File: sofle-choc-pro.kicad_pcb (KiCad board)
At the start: 4 copper layers, 129 x 119 mm, 198 parts, among them J1 Connector, USB-TYPE-C-16P, J2 Connector, USB-TYPE-C-16P, J3 OLED 128x32 / nice!view, SW1 BOOT, SW10 F0, SW11 F1, SW12 F2, SW13 F3, SW14 F4, SW15 F5, SW16 F6 Choc/EC11, SW2 RESET, SW20 N0, SW21 N1, SW22 N2, SW23 N3, SW24 N4, SW25 N5, SW30 T0, SW31 T1, SW32 T2, SW33 T3, SW34 T4, SW35 T5, SW40 H0, SW41 H1, SW42 H2, SW43 H3, SW44 H4, SW45 H5, SW50 B0, SW51 B1, SW52 B2, SW53 B3, SW54 B4, SW55 B5, SW60 TH0, SW61 TH1, SW62 TH2, SW63 TH3, SW64 TH4, SW65 TH5 Choc/EC11, U1 RP2040, U2 SRV05-4, U3 W25Q128, U4 SRV05-4, U5 AP2112K-3.3, U6 SN74LV1T34DBVR, X1 ABM8-272-T3

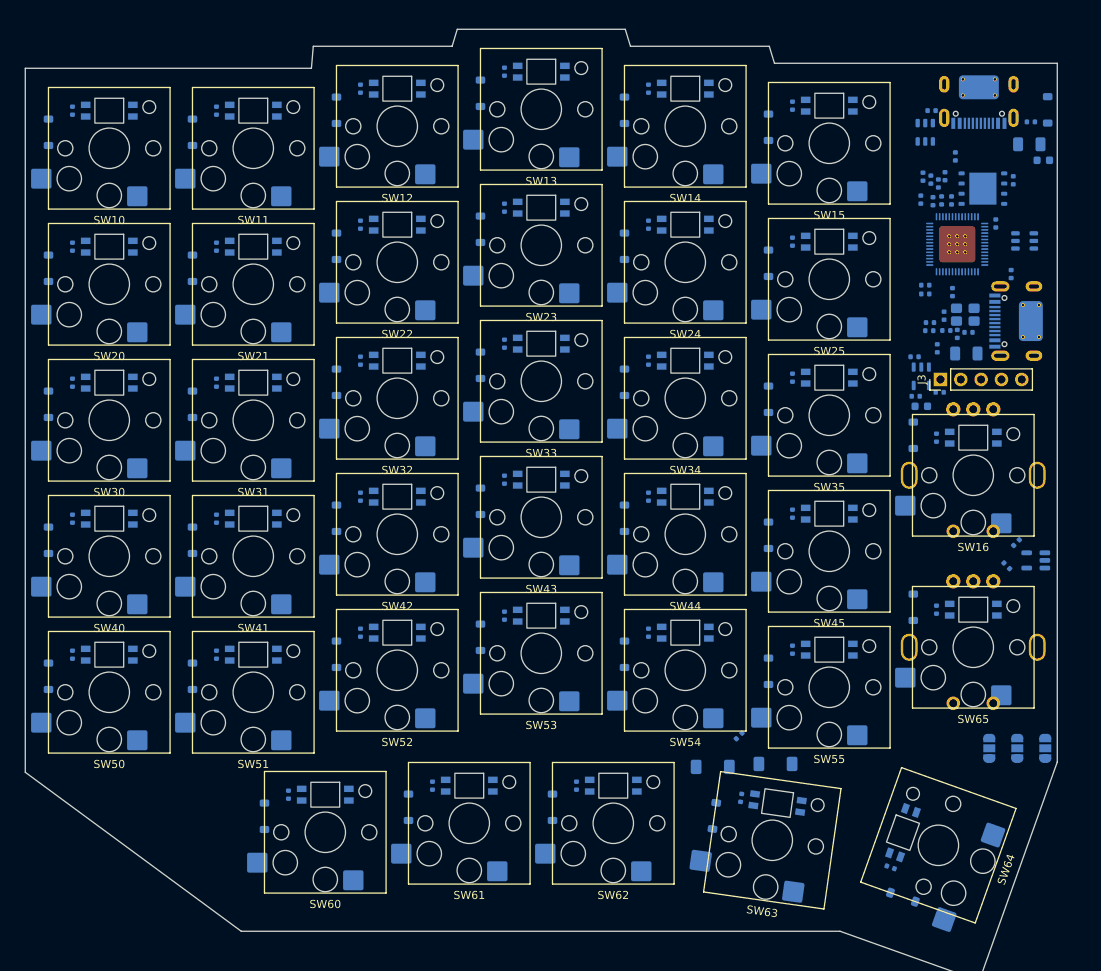
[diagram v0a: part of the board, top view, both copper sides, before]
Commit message: feat(pcb): swap usb-c and esd parts, fix nets, rules and silkscreen
Moves both USB-C ports to the part every reference board uses, shrinks the
ESD arrays and cleans up the nets, rules and silkscreen around them. The
board passes ERC and DRC with no errors and no schematic parity issues.

- USB-C J1/J2 are now HRO TYPE-C-31-M-12 (LCSC C165948), the connector the
  RP2040 design guide, Corne v4, Djinn, Ferris and sea-picro all use, with
  its real 3D model and a project footprint whose pad numbers match our
  symbol; both sit 0.49 mm proud of the board edge, per its datasheet
- ESD arrays are USBLC6-2P6 in SOT-563 (2.0 x 2.5 mm against 3.1 x 2.1),
  and their two channels now carry each data line through the part, which
  is the layout ST and TI ask for
- USB nets are named per segment so each side of R7/R8 is its own net:
  D+/D- from the connector, USB_P/USB_N into the MCU
- R7/R8 moved 12.7 mm clear of U1 so the MCU-side labels have a wire to sit
  on instead of printing over the chip symbol
- protection parts sit at the connectors: fuse 2.5 mm from the 5 V pad,
  ESD 1.5 to 2.0 mm from the data pads, diode right after the fuse
- fuses raised to 1.1 A (LCSC C126818): 37 LEDs at the planned brightness
  draw about 0.8 A through one half's fuse, which would trip a 500 mA part

Under the hood:

- design rules follow JLCPCB's published limits: 0.3 mm copper to edge,
  0.4 mm minimum via, 0.15 mm silkscreen lines and 1.0 mm text
- one diff pair rule per pair, with spacing checked outside the fan-out and
  length across the whole net; a shared rule compared nets across ports,
  and a rule condition split over two lines was silently ignored
- no pair rule on the link port: it is one-wire serial, and LINK_D_N never
  reaches the MCU
- GND plane moved to the inner layer next to the parts, so USB, ESD and
  decoupling reference solid ground
- crystal keep-out now covers the power plane only: Abracon and Raspberry
  Pi ask for short traces, not cleared ground, and the plane a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
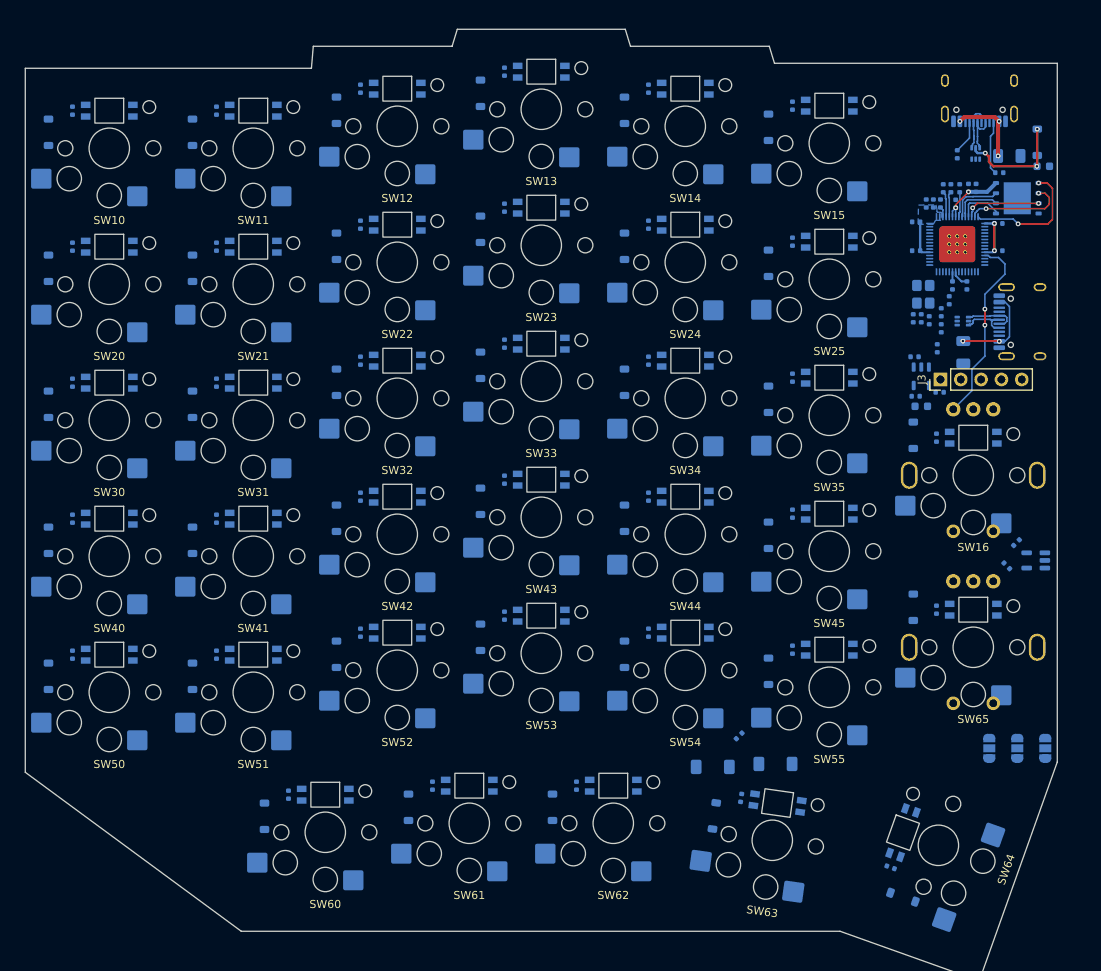
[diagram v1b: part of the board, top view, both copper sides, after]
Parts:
- F1, F2: value 500mA -> 1.1A
- J1, J2: footprint PCM_JLCPCB:TYPE-C-SMD_HX-TYPE-C-16PIN -> my-soffle:USB_C_Receptacle_HRO_TYPE-C-31-M-12_MergedPads
- U2, U4: value SRV05-4 -> USBLC6-2P6; footprint PCM_JLCPCB:SOT-23-6_L2.9-W1.6-P0.95-LS2.9-BL -> Package_TO_SOT_SMD:SOT-563
- U3: value W25Q128 -> W25Q128JVPIQ
- moved U2 12.7 mm to (166.7, 93.6), turned to 0 degrees
- moved C13 8.85 mm to (160.9, 84.8), turned to 180 degrees
- moved R6 7.48 mm to (171.2, 75.0)
- moved U4 6.83 mm to (168.3, 72.7), turned to 90 degrees
- moved R5 6.33 mm to (166.0, 72.8), turned to -90 degrees
- moved X1 5.84 mm to (161.8, 90.2), turned to 90 degrees
- moved R11 5.84 mm to (160.5, 93.2), turned to -90 degrees
- moved C14 5.59 mm to (160.9, 81.2), turned to 180 degrees
- moved C12 5.31 mm to (167.2, 89.1), turned to -90 degrees
- moved C6 5.06 mm to (166.3, 77.0)
- moved C3 4.75 mm to (168.3, 77.0)
- moved U3 4.47 mm to (173.5, 78.2)
- moved C15 4.26 mm to (167.4, 77.0)
- moved D1 4.25 mm to (176.0, 71.2), turned to -90 degrees
- moved C1 4.23 mm to (164.0, 92.5), turned to 90 degrees
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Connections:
- net USB_MCU_N renamed USB_N
- net USB_MCU_P renamed USB_P
- J1 pad A6: D_USB_P -> D+
- J1 pad A7: D_USB_N -> D-
- J1 pad B6: D_USB_P -> D+
- J1 pad B7: D_USB_N -> D-
- R7 pad 1: D_USB_P -> D+
- R8 pad 1: D_USB_N -> D-
- U2 pad 3: unconnected-(U2-I/O-Pad3) -> LINK_D_N
- U2 pad 6: unconnected-(U2-I/O-Pad6) -> LINK_D_P
- U4 pad 1: D_USB_P -> D+
- U4 pad 3: unconnected-(U4-I/O-Pad3) -> D-
- U4 pad 4: unconnected-(U4-I/O-Pad4) -> D-
- U4 pad 6: D_USB_N -> D+
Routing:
- net GP8: track 0.00 -> 23.8 mm, vias 0 -> 2
- net +3.3V: track 0.00 -> 21.9 mm, vias 0 -> 4
- net SS: track 0.00 -> 15.8 mm, vias 0 -> 2
- net +5V: track 0.00 -> 13.9 mm, vias 0 -> 3
- net SD1: track 0.00 -> 12.8 mm, vias 0 -> 2
- net LINK_VBUS: track 0.00 -> 11.4 mm, vias 0 -> 2
- net VBUS: track 0.00 -> 9.73 mm, vias 0 -> 3
- net SD2: track 0.00 -> 9.63 mm, vias 0 -> 2
- net LINK_D_P: track 0.00 -> 6.92 mm
- net Net-(J1-CC2): track 0.00 -> 6.82 mm
- net SD3: track 0.00 -> 6.63 mm
- net LINK_D_N: track 0.00 -> 6.50 mm
- net D-: track 0.00 -> 6.04 mm
- net D+: track 0.00 -> 6.03 mm
- net CLK: track 0.00 -> 5.98 mm
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- added copper zone on B.Cu, net +3.3V
- added copper zone on In1.Cu, net +3.3V
- added copper zone on In1.Cu, net +5V
- added copper zone on In2.Cu, net GND
- removed copper zone on In2.Cu, net +3.3V
- removed copper zone on In2.Cu, net +5V
- removed copper zone on In1.Cu, net GND

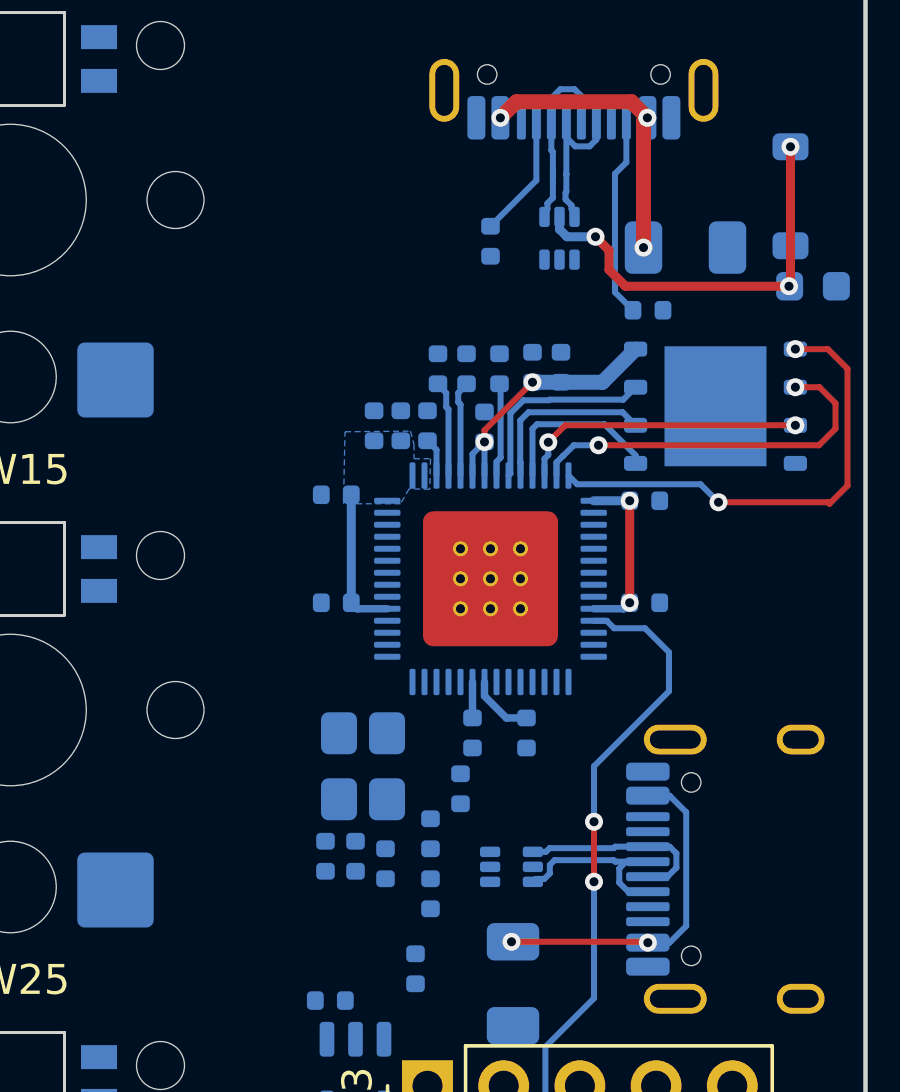
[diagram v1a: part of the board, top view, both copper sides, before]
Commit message: fix(pcb): drop the dead link d- pad and exempt the esd fan-out
The link between halves is one-wire serial, so D- stops at the ESD array.
Both of its pads carried the net, which left KiCad asking for copper between
two pins the chip already joins inside. Now only the pad the connector
reaches is wired, and the other is a no-connect.

- U2 pin 3 disconnected in the schematic and on the board: four fewer
  unconnected items, and no more phantom pad-to-pad link
- D+/D- spacing rule now skips U4's courtyard as well as J1's and U1's,
  since the ESD array's two data pins sit 2.3 mm apart and set the gap

Also carries the USB and link routing done in KiCad since the last commit.

ERC 0 errors. DRC 0 errors, 0 parity issues. One skew flag remains on the
host pair (0.23 mm), to even out once that pair is finished.
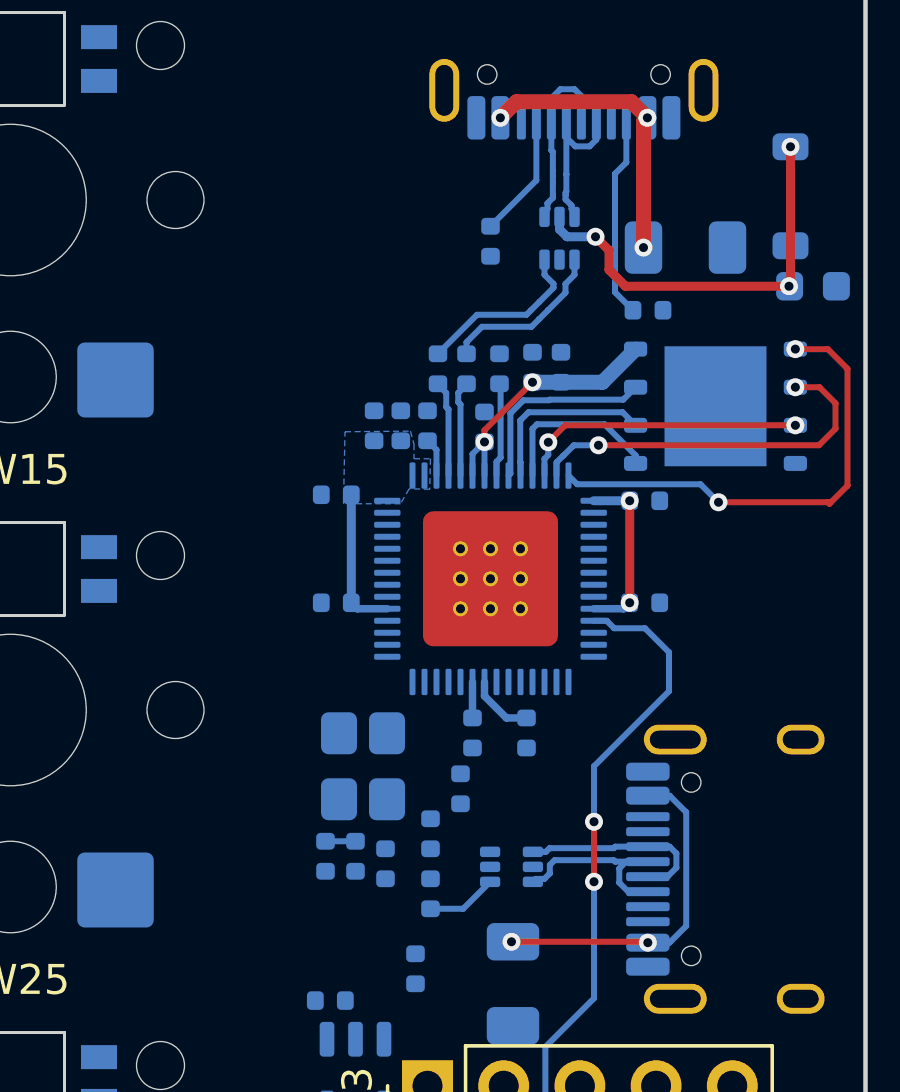
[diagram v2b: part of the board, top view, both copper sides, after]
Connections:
- U2 pad 3: LINK_D_N -> (no net)
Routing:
- net D-: track 6.04 -> 11.9 mm
- net D+: track 6.03 -> 11.6 mm
- net LINK_D_P: track 6.92 -> 9.28 mm
- net GP13: track 0.00 -> 1.00 mm
